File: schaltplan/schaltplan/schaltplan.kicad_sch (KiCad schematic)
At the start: 9 parts, among them SW1 SW_Nidec_CAS-120A1, U1 DFR0478

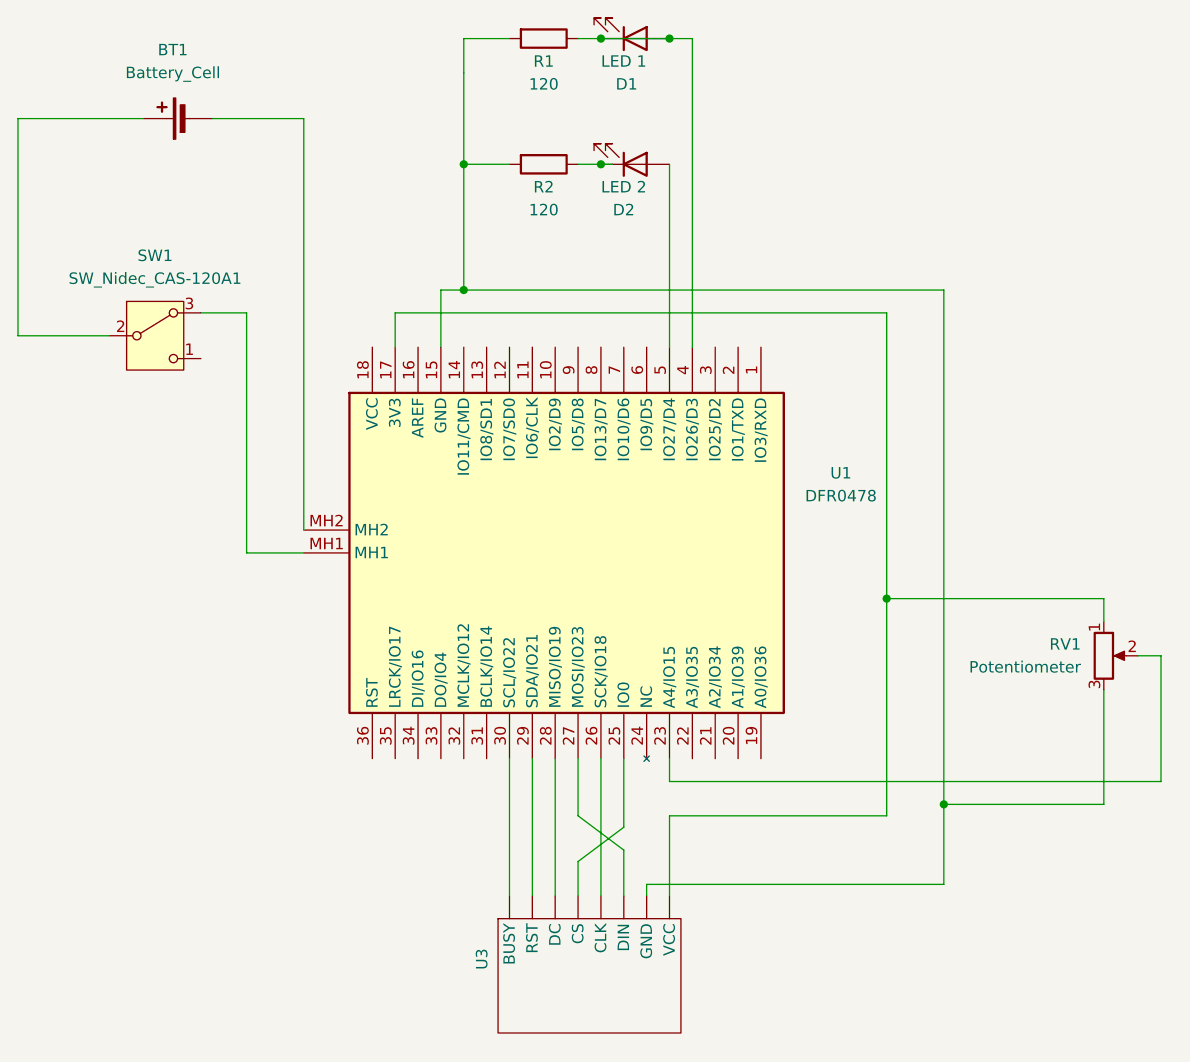
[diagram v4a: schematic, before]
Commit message: Schaltplan aktualisiert mit DS18B20 (Temperatursensor) und Joystick
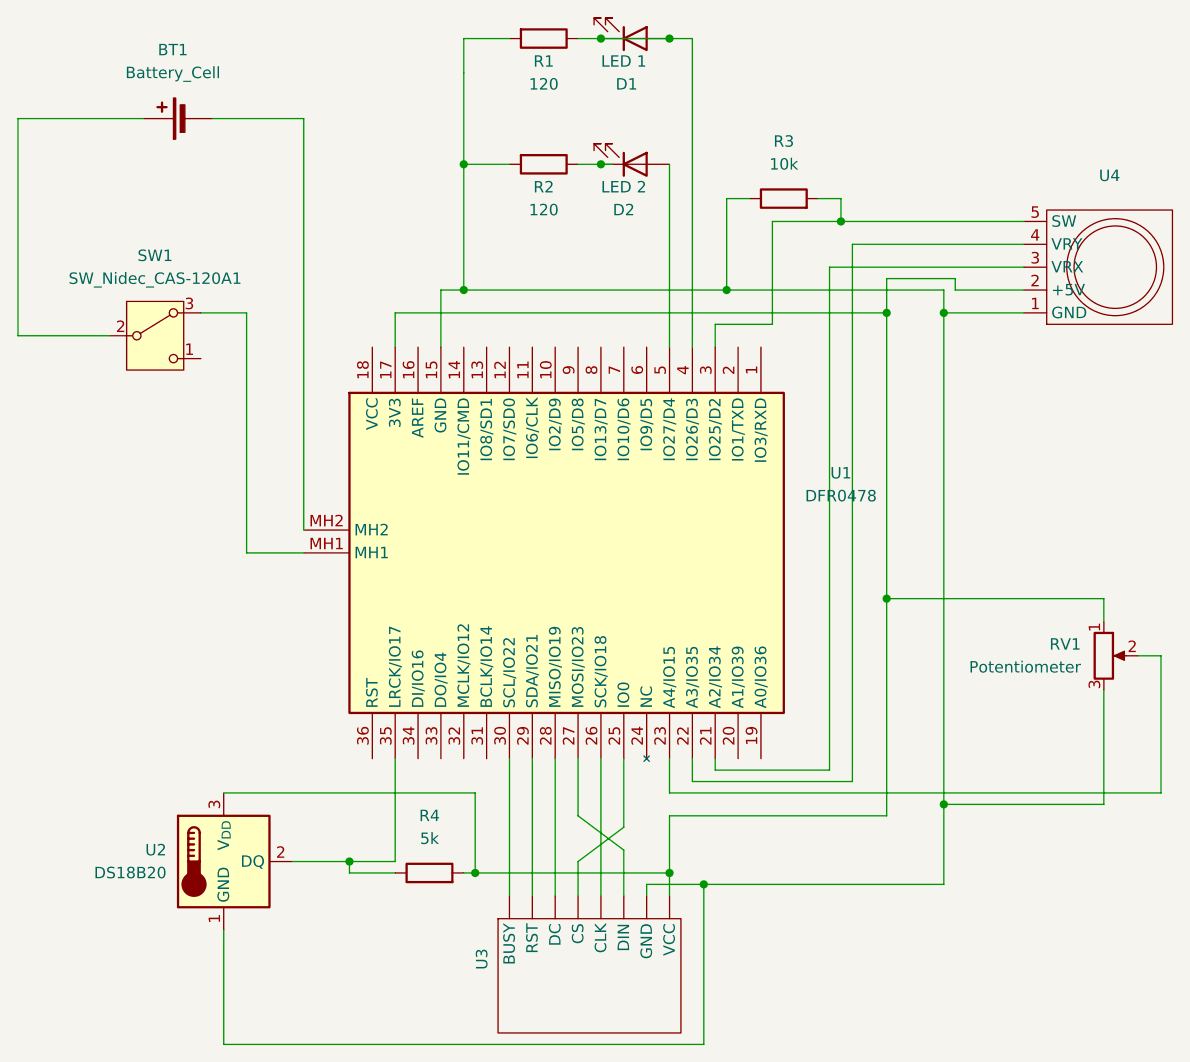
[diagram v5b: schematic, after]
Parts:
- added R3: 10k, symbol Device:R
- added R4: 5k, symbol Device:R
- added U2: DS18B20, Package_TO_SOT_THT:TO-92_Inline, symbol Sensor_Temperature:DS18B20
- added U4: ~, symbol Custom_Components:Joystick
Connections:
- net at R1.2, R2.2, RV1.3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: now also R3.1, U2.1 (GND), U4.1 (GND)
- net at RV1.1, U1.17 (3V3), U3. (VCC): now also R4.2, U2.3 (V_{DD}), U4.2 (+5V)
- net at U1.21 (A2/IO34): now also U4.3 (VRX)
- net at U1.22 (A3/IO35): now also U4.4 (VRY)
- net at U1.3 (IO25/D2): now also R3.2, U4.5 (SW)
- net at U1.35 (LRCK/IO17): now also R4.1, U2.2 (DQ)

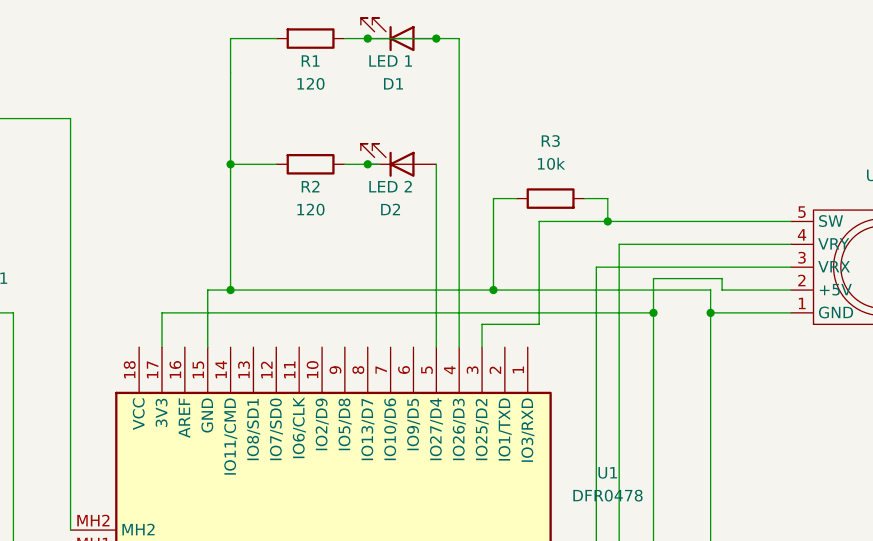
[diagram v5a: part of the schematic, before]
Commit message: Kleinen Fehler behoben: Der Widerstand vom Joystick muss auf + geschaltet werden
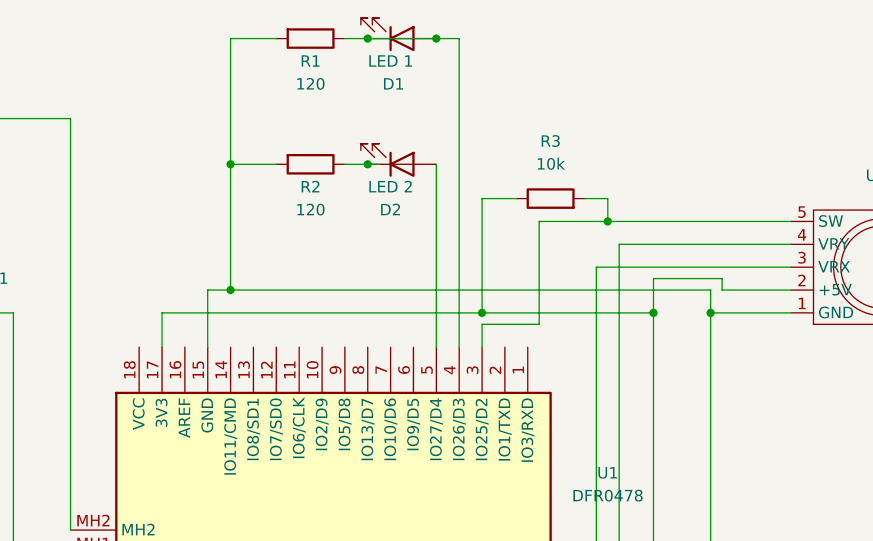
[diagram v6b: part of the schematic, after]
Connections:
- net at R1.2, R2.2, RV1.3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: no longer R3.1
- net at R4.2, RV1.1, U1.17 (3V3)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: now also R3.1
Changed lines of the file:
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@@
-	)
-	(junction
-		(at 96.52 69.85)
-		(diameter 0)
-		(color 0 0 0 0)
 	)
 	(junction
@@
 		(color 0 0 0 0)
 	)
+	(junction
+		(at 95.25 72.39)
+		(diameter 0)
+		(color 0 0 0 0)
+	)
 	(wire
 		(pts
@@
 	(wire
 		(pts
-			(xy 96.52 69.85) (xy 96.52 59.69)
-		)
-		(stroke
-			(width 0)
-			(type default)
-			(color 0 0 0 1)
-		)
-	)
-	(wire
-		(pts
 			(xy 82.55 55.88) (xy 83.82 55.88)
 		)
@@
 	(wire
 		(pts
-			(xy 96.52 59.69) (xy 99.06 59.69)
-		)
-		(stroke
-			(width 0)
-			(type default)
-			(color 0 0 0 1)
-		)
-	)
-	(wire
-		(pts
 			(xy 101.6 62.23) (xy 101.6 73.66)
 		)
@@
 	(wire
 		(pts
-			(xy 59.69 72.39) (xy 114.3 72.39)
-		)
-		(stroke
-			(width 0)
-			(type default)
-			(color 255 0 9 1)
-		)
-	)
-	(wire
-		(pts
 			(xy 31.75 50.8) (xy 17.78 50.8)
 		)
@@
 	(wire
 		(pts
+			(xy 59.69 72.39) (xy 95.25 72.39)
+		)
+		(stroke
+			(width 0)
+			(type default)
+			(color 255 0 9 1)
+		)
+	)
+	(wire
+		(pts
 			(xy 90.17 134.62) (xy 90.17 137.16)
 		)
@@
 	(wire
 		(pts
+			(xy 95.25 72.39) (xy 114.3 72.39)
+		)
+		(stroke
+			(width 0)
+			(type default)
+			(color 255 0 9 1)
+		)
+	)
+	(wire
+		(pts
 			(xy 85.09 132.08) (xy 85.09 137.16)
 		)
@@
 	(wire
 		(pts
-			(xy 96.52 69.85) (xy 120.65 69.85)
-		)
-		(stroke
-			(width 0)
-			(type default)
-			(color 0 0 0 1)
+			(xy 67.31 69.85) (xy 120.65 69.85)
+		)
+		(stroke
+			(width 0)
+			(type default)
+			(color 0 0 0 1)
+		)
+	)
+	(wire
+		(pts
+			(xy 95.25 72.39) (xy 95.25 59.69)
+		)
+		(stroke
+			(width 0)
+			(type default)
+			(color 255 0 9 1)
 		)
 	)
@@
 	(wire
 		(pts
+			(xy 95.25 59.69) (xy 99.06 59.69)
+		)
+		(stroke
+			(width 0)
+			(type default)
+			(color 255 0 9 1)
+		)
+	)
+	(wire
+		(pts
 			(xy 120.65 127) (xy 120.65 135.89)
 		)
@@
 		)
 		(stroke
-			(width 0)
-			(type default)
-			(color 0 0 0 1)
-		)
-	)
-	(wire
-		(pts
-			(xy 67.31 69.85) (xy 96.52 69.85)
-		)
-		(stroke

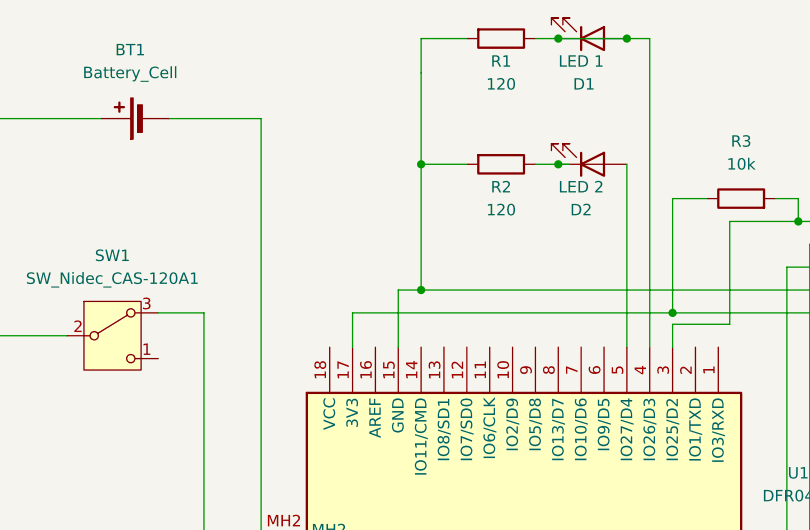
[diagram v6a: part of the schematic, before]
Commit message: Buzzer auf dem Schaltplan hinzugefügt
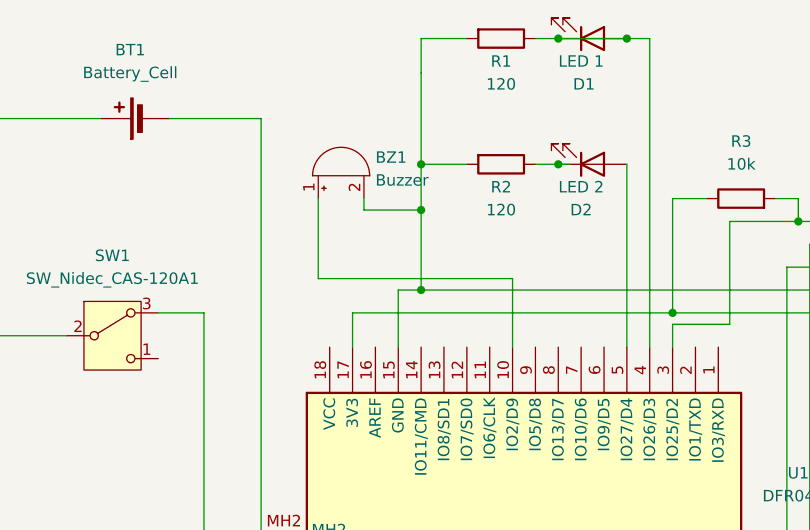
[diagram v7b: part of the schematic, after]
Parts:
- added BZ1: Buzzer, symbol Device:Buzzer
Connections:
- net at R1.2, R2.2, RV1.3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: now also BZ1.2 (-)
- net at U1.10 (IO2/D9): now also BZ1.1 (+)
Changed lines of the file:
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@@
+	)
+	(junction
+		(at 67.31 60.96)
+		(diameter 0)
+		(color 0 0 0 0)
 	)
 	(junction
@@
 	(wire
 		(pts
+			(xy 77.47 68.58) (xy 77.47 76.2)
+		)
+		(stroke
+			(width 0)
+			(type default)
+		)
+	)
+	(wire
+		(pts
 			(xy 67.31 134.62) (xy 68.58 134.62)
 		)
@@
 	(wire
 		(pts
+			(xy 67.31 60.96) (xy 60.96 60.96)
+		)
+		(stroke
+			(width 0)
+			(type default)
+			(color 0 0 0 1)
+		)
+	)
+	(wire
+		(pts
 			(xy 95.25 121.92) (xy 95.25 123.19)
 		)
@@
 	(wire
 		(pts
-			(xy 67.31 55.88) (xy 67.31 69.85)
+			(xy 67.31 55.88) (xy 67.31 60.96)
 		)
 		(stroke
@@
 	(wire
 		(pts
+			(xy 55.88 68.58) (xy 77.47 68.58)
+		)
+		(stroke
+			(width 0)
+			(type default)
+		)
+	)
+	(wire
+		(pts
 			(xy 68.58 134.62) (xy 90.17 134.62)
 		)
@@
 	(wire
 		(pts
+			(xy 55.88 59.69) (xy 55.88 68.58)
+		)
+		(stroke
+			(width 0)
+			(type default)
+		)
+	)
+	(wire
+		(pts
 			(xy 120.65 127) (xy 120.65 72.39)
 		)
@@
 	(wire
 		(pts
+			(xy 60.96 59.69) (xy 60.96 60.96)
+		)
+		(stroke
+			(width 0)
+			(type default)
+			(color 0 0 0 1)
+		)
+	)
+	(wire
+		(pts
 			(xy 93.98 135.89) (xy 93.98 153.67)
 		)
@@
 		(pts
 			(xy 67.31 69.85) (xy 120.65 69.85)
+		)
+		(stroke
+			(width 0)
+			(type default)
+			(color 0 0 0 1)
+		)
+	)
+	(wire
+		(pts
+			(xy 67.31 60.96) (xy 67.31 69.85)
 		)
 		(stroke
@@
 					(unit 1)
 				)
+			)
+		)
+	)
+	(symbol
+		(lib_id "Device:Buzzer")
+		(at 58.42 57.15 90)
+		(unit 1)
+		(exclude_from_sim no)
+		(in_bom yes)
+		(on_board yes)
+		(dnp no)
+		(fields_autoplaced yes)
+		(property "Reference" "BZ1"
+			(at 62.23 55.1248 90)
+			(effects
+				(font
+					(size 1.27 1.27)
+				)
+				(justify right)
+			)
+		)
+		(property "Value" "Buzzer"
+			(at 62.23 57.6648 90)
+			(effects
+				(font
+					(size 1.27 1.27)
+				)
+				(justify right)
+			)
+		)
+		(property "Footprint" ""
+			(at 55.88 57.785 90)
+			(effects
+				(font
+					(size 1.27 1.27)
+				)
+				(hide yes)
+			)
+		)
+		(property "Datasheet" "~"
+			(at 55.88 57.785 90)
+			(effects
+				(font
+					(size 1.27 1.27)
+				)
+				(hide yes)
+			)
+		)
+		(property "Description" "Buzzer, polarized"
+			(at 58.42 57.15 0)
+			(effects
+				(font
+					(size 1.27 1.27)
+				)
+				(hide yes)
+			)
+		)
+		(pin "2"
+		)
+		(pin "1"
+		)
+		(instances
+			(project ""
+				(path "/f79f94d7-572e-4250-b494-96d40f946eb3"
+					(reference "BZ1")
+					(unit 1)
+				)

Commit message: bezeichnung eingefügt
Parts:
- Potentiometer: renamed from RV1; value Potentiometer -> ~
- renumbered U3 to Display, U2 to S1
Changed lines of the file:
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@@
 		(on_board yes)
 		(dnp no)
-		(property "Reference" "U3"
+		(property "Reference" "Display"
 			(at 69.342 143.002 0)
 			(effects
@@
 			(project ""
 				(path "/f79f94d7-572e-4250-b494-96d40f946eb3"
-					(reference "U3")
+					(reference "Display")
 					(unit 1)
 				)
@@
 		(on_board yes)
 		(dnp no)
-		(fields_autoplaced yes)
-		(property "Reference" "U2"
-			(at 34.29 132.0799 0)
+		(property "Reference" "S1"
+			(at 34.29 130.81 0)
 			(effects
 				(font
@@
 		)
 		(property "Value" "DS18B20"
-			(at 34.29 134.6199 0)
+			(at 34.29 133.35 0)
 			(effects
 				(font
@@
 			(project ""
 				(path "/f79f94d7-572e-4250-b494-96d40f946eb3"
-					(reference "U2")
+					(reference "S1")
 					(unit 1)
 				)
@@
 		(on_board yes)
 		(dnp no)
-		(fields_autoplaced yes)
 		(property "Reference" "U1"
-			(at 109.22 90.2014 0)
+			(at 97.79 96.52 0)
 			(effects
 				(font
@@
 		)
 		(property "Value" "DFR0478"
-			(at 109.22 92.7414 0)
+			(at 97.79 100.33 0)
 			(effects
 				(font
@@
 		(dnp no)
 		(fields_autoplaced yes)
-		(property "Reference" "RV1"
-			(at 135.89 109.2199 0)
+		(property "Reference" "Potentiometer"
+			(at 135.89 109.8549 0)
 			(effects
 				(font
@@
 			)
 		)
-		(property "Value" "Potentiometer"
-			(at 135.89 111.7599 0)
+		(property "Value" "~"
+			(at 135.89 111.76 0)
 			(effects
 				(font
@@
 			(project ""
 				(path "/f79f94d7-572e-4250-b494-96d40f946eb3"
-					(reference "RV1")
-					(unit 1)
-				)
+					(reference "Potentiometer")
+					(unit 1)
+				)
